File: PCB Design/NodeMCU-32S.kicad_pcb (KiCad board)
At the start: 2 copper layers, 85.4 x 61.5 mm, 23 parts, among them J1 Screw_Terminal_01x02, J2 Screw_Terminal_01x02, J3 Screw_Terminal_01x02, J4 Screw_Terminal_01x02, J5 Screw_Terminal_01x03, J6 Screw_Terminal_01x02, Q1 IRLZ44N, Q2 2N2646, SW1 SW_DPDT_x2, U1 ESP32-DevKitC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

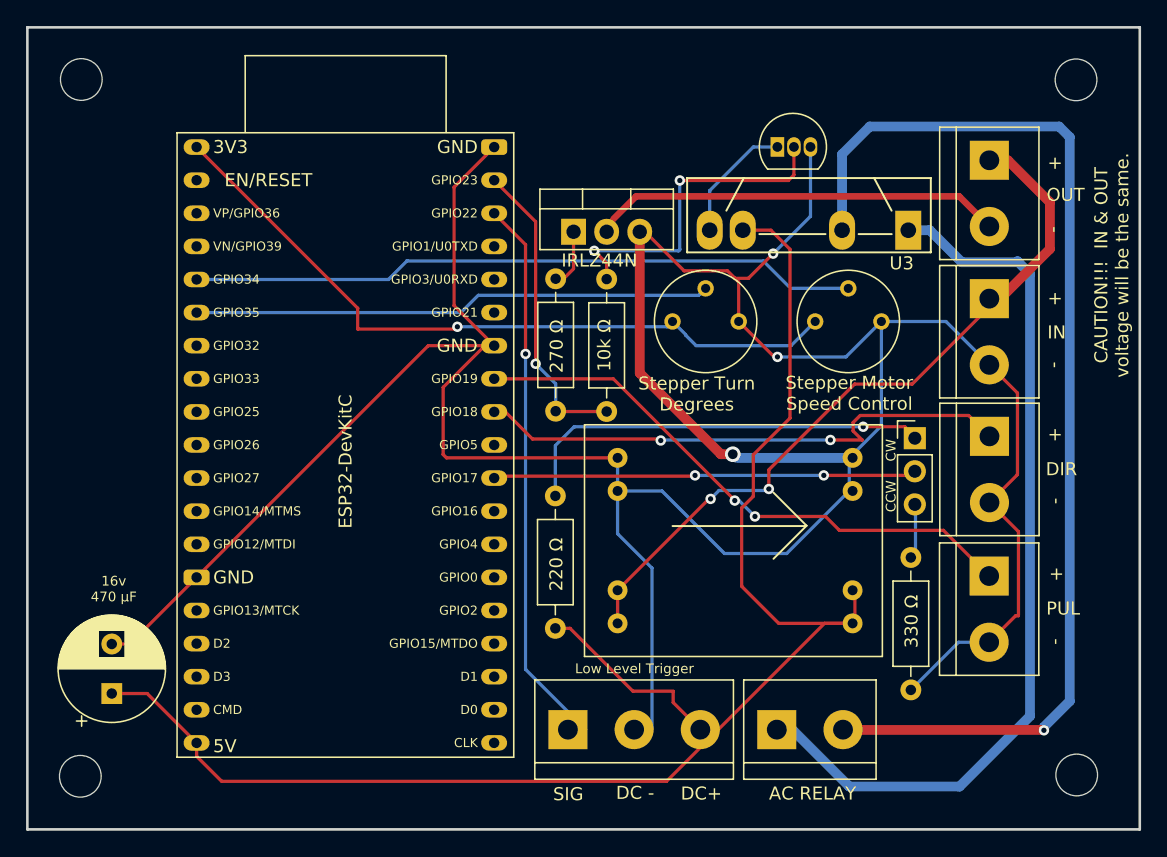
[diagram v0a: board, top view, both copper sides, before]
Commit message: Updated Photos and Voltage Divider
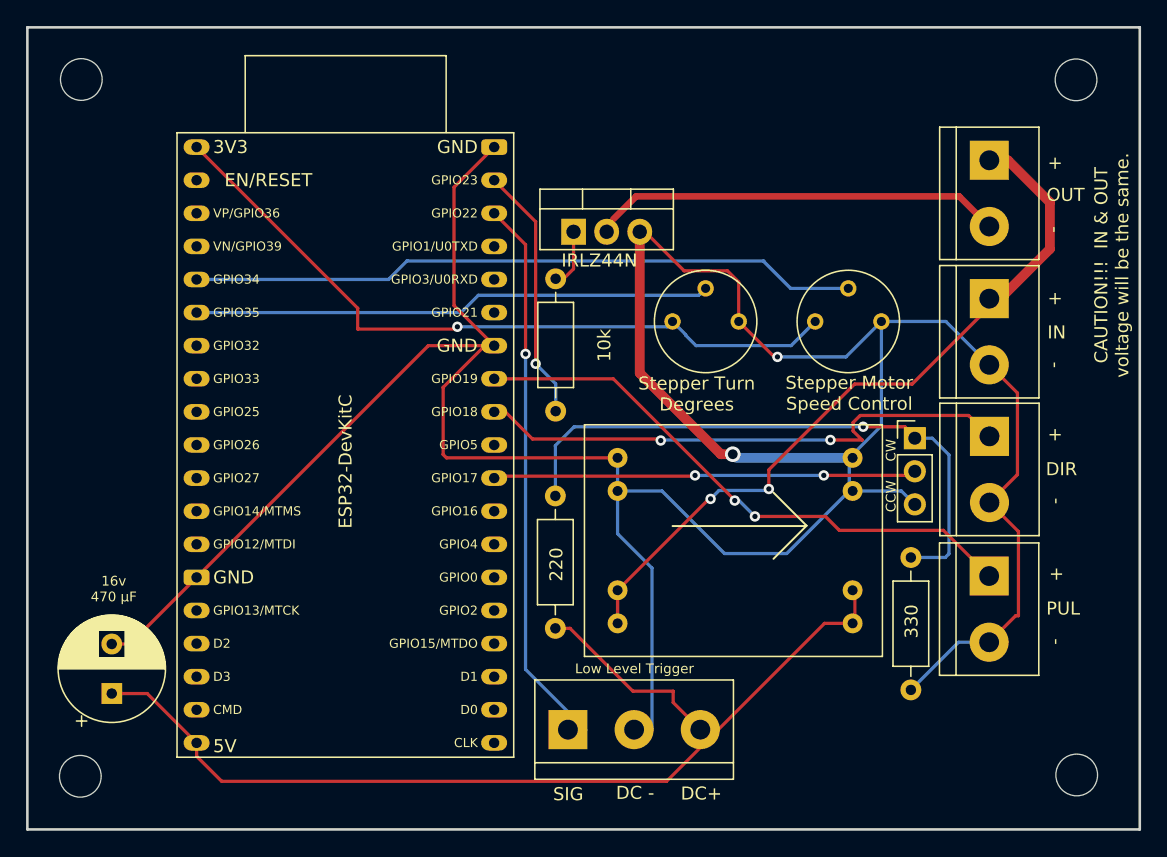
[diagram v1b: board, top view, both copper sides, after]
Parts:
- removed J6: Screw_Terminal_01x02, TerminalBlock:TerminalBlock_bornier-2_P5.08mm
- removed Q2: 2N2646, Package_TO_SOT_THT:TO-92L_Inline
- removed R2: 270 Ω, Resistor_THT:R_Axial_DIN0207_L6.3mm_D2.5mm_P10.16mm_Horizontal
- removed U3: S216S01, Package_SIP:SIP4_Sharp-SSR_P7.62mm_Straight
- R1: value 10k Ω -> 10k
- R3: value 220 Ω -> 220
- R4: value 330 Ω -> 330
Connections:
- R4 pad 1: Net-(R4-Pad1) -> Net-(R3-Pad2)
- SW1 pad 3: Net-(R4-Pad1) -> GND
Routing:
- net AC_2: track 86.3 -> 0.00 mm, vias 1 -> 0
- net AC_1: track 68.2 -> 0.00 mm
- net +5V: track 123.8 -> 82.7 mm
- net Net-(Q2-Pad2): track 25.6 -> 0.00 mm, vias 2 -> 0
- net Net-(R3-Pad2): track 32.4 -> 46.2 mm
- net SSR_GND: track 9.62 -> 0.00 mm
- net GND: track 248.6 -> 240.7 mm, vias 3 -> 2
- net Net-(R4-Pad1): track 4.29 -> 0.00 mm
- net highActivationPin: track 23.2 -> 19.8 mm
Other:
- board text removed: "AC RELAY"

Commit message: reversed map function, fixed spelling errors, cleaned board.
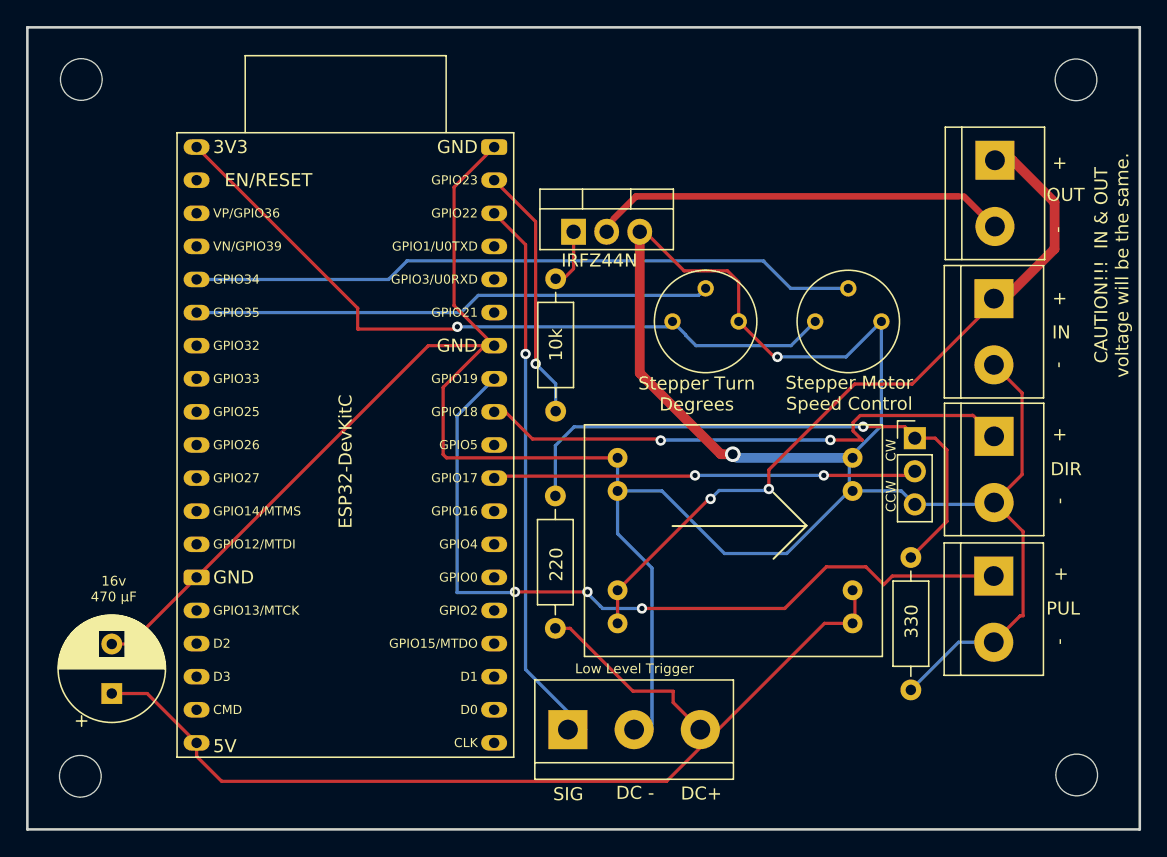
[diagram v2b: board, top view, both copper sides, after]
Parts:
- Q1: value IRLZ44N -> IRFZ44N
- moved J1 0.43 mm to (133.7, 62.0)
- moved J4 0.36 mm to (133.6, 93.9)
- moved J2 0.36 mm to (133.6, 72.6)
- moved J3 0.36 mm to (133.6, 83.2)
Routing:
- net PUL: track 44.3 -> 61.5 mm, vias 2 -> 3
- net GND: track 240.7 -> 237.5 mm
- net Net-(R3-Pad2): track 46.2 -> 44.7 mm
- net VCC: track 57.4 -> 56.7 mm
